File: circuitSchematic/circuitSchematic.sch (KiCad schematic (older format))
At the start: 7 parts, among them J1 MC912C128, U10 74LS138, U12 74HCT238, U14 OPT101, U15 KWM-30881AVB

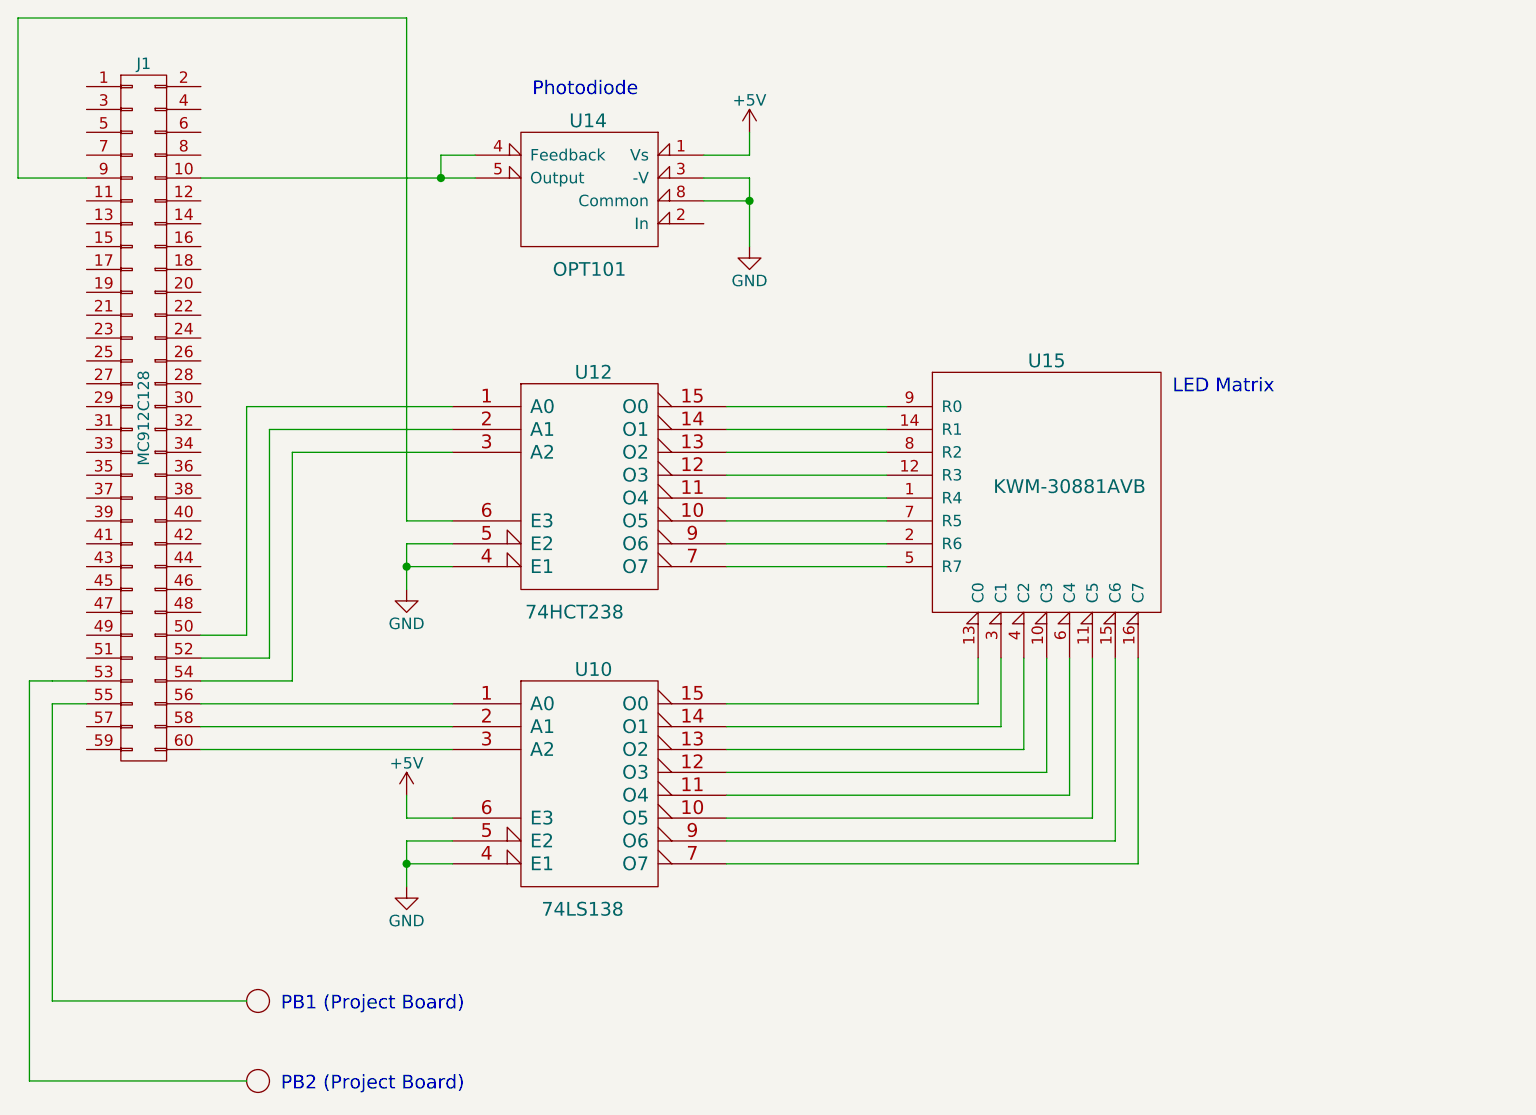
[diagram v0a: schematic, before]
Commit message: Added in the circuit schematic with resistors. Updated the kicad project appropiately.
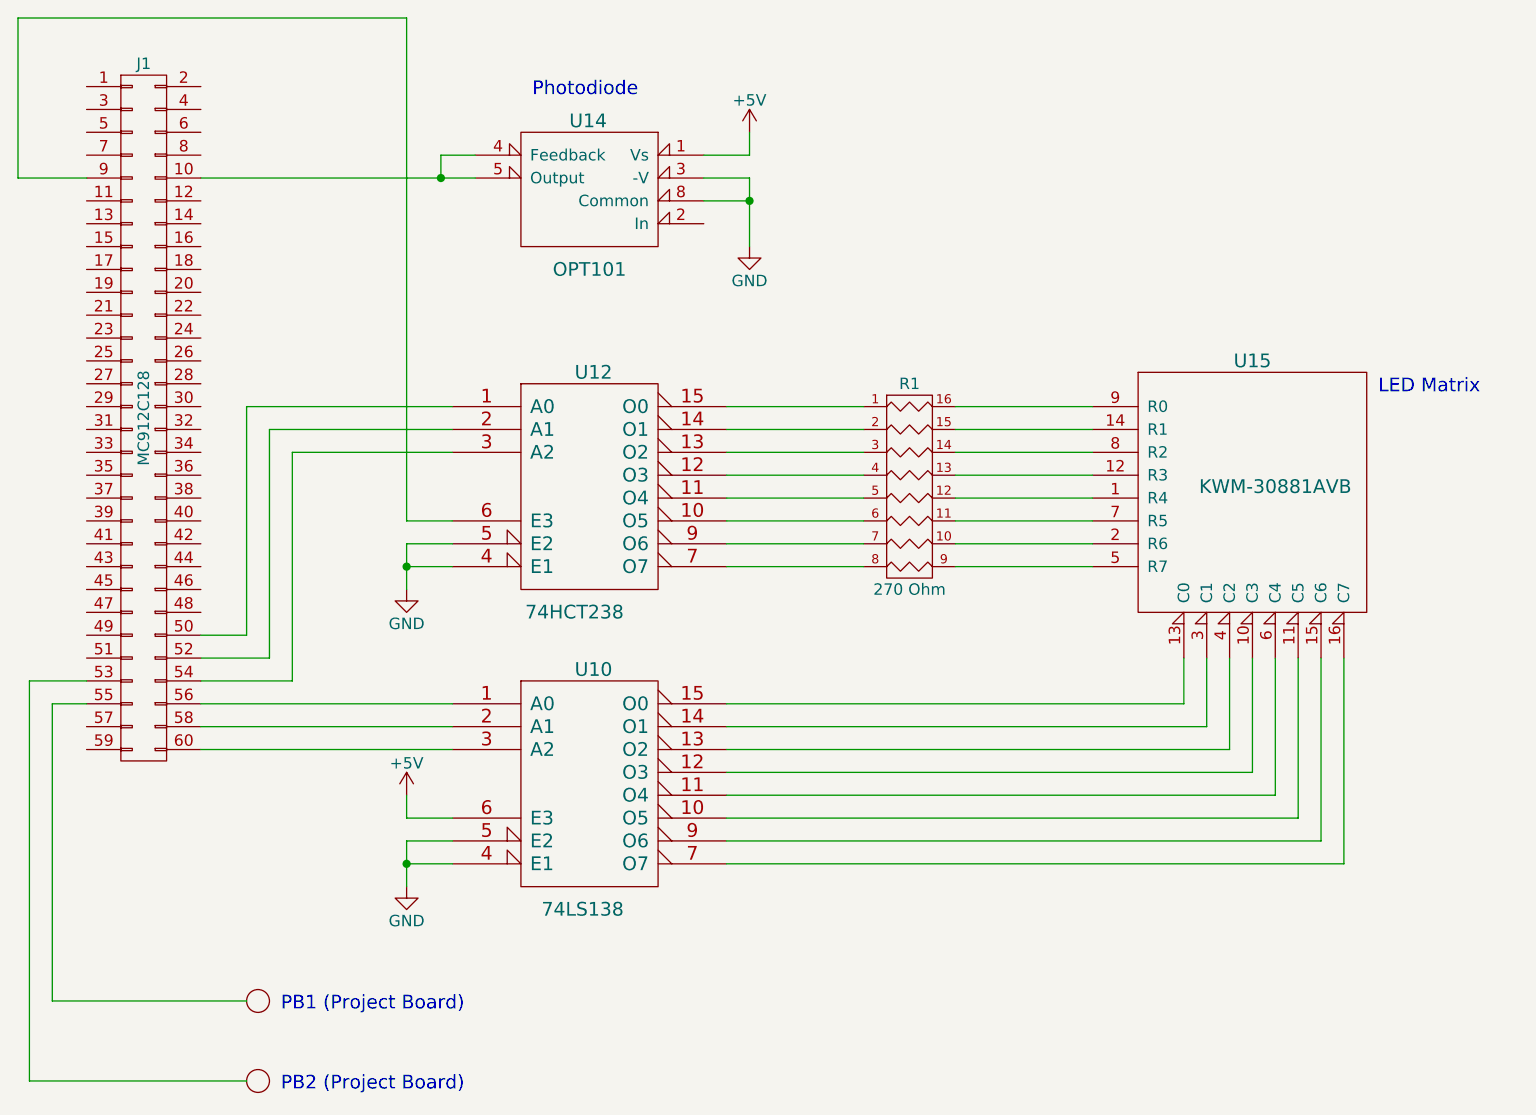
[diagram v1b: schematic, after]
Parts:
- added R1: 270 Ohm, symbol R_PACK8
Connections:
- wire segments 68 -> 71
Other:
- moved on the sheet: U15
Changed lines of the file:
@@
 L KWM-30881AVB U15
 U 1 1 554BE190
-P 5300 3650
-F 0 "U15" H 5300 4200 60  0000 C CNN
-F 1 "KWM-30881AVB" H 5400 3650 60  0000 C CNN
-F 2 "" H 5400 3650 60  0000 C CNN
-F 3 "" H 5400 3650 60  0000 C CNN
-	1    5300 3650
+P 6200 3650
+F 0 "U15" H 6200 4200 60  0000 C CNN
+F 1 "KWM-30881AVB" H 6300 3650 60  0000 C CNN
+F 2 "" H 6300 3650 60  0000 C CNN
+F 3 "" H 6300 3650 60  0000 C CNN
+	1    6200 3650
 	1    0    0    -1
 $EndComp
@@
 	1    0    0    -1
 $EndComp
-Text Notes 5850 3250 0    60   ~ 0
+Text Notes 6750 3250 0    60   ~ 0
 LED Matrix
 $Comp
@@
 	-1   0    0    -1
 $EndComp
-Wire Wire Line
-	1600 2300 2650 2300
-Wire Wire Line
-	2650 2300 2800 2300
-Wire Wire Line
-	850  6250 1800 6250
-Wire Wire Line
-	850  4500 850  6250
-Wire Wire Line
-	1100 4500 950  4500
-Wire Wire Line
-	950  4500 850  4500
-Wire Wire Line
-	950  5900 1800 5900
-Wire Wire Line
-	950  4600 950  5900
-Wire Wire Line
-	1100 4600 950  4600
-Wire Wire Line
-	2500 3800 2700 3800
-Wire Wire Line
-	2500 1600 2500 3800
-Wire Wire Line
-	800  1600 2500 1600
-Wire Wire Line
-	800  2300 800  1600
-Wire Wire Line
-	1100 2300 800  2300
-Connection ~ 2500 4000
-Wire Wire Line
-	2700 3900 2500 3900
-Wire Wire Line
-	2500 3900 2500 4000
-Wire Wire Line
-	2500 4000 2500 4100
-Wire Wire Line
-	2700 4000 2500 4000
-Wire Wire Line
-	2500 5100 2500 5000
-Wire Wire Line
-	2700 5100 2500 5100
-Connection ~ 2500 5300
-Wire Wire Line
-	2700 5200 2500 5200
-Wire Wire Line
-	2500 5200 2500 5300
-Wire Wire Line
-	2500 5300 2500 5400
-Wire Wire Line
-	2700 5300 2500 5300
-Wire Wire Line
-	1800 3300 2700 3300
-Wire Wire Line
-	1800 4300 1800 3300
-Wire Wire Line
-	1600 4300 1800 4300
-Wire Wire Line
-	1900 3400 2700 3400
-Wire Wire Line
-	1900 4400 1900 3400
-Wire Wire Line
-	1600 4400 1900 4400
-Wire Wire Line
-	2000 3500 2700 3500
-Wire Wire Line
-	2000 4500 2000 3500
-Wire Wire Line
-	1600 4500 2000 4500
-Wire Wire Line
-	1600 4600 2700 4600
-Wire Wire Line
-	1600 4700 2700 4700
-Wire Wire Line
-	1600 4800 2700 4800
-Wire Wire Line
-	5700 5300 5700 4400
-Wire Wire Line
-	3900 5300 5700 5300
-Wire Wire Line
-	5600 5200 5600 4400
-Wire Wire Line
-	3900 5200 5600 5200
-Wire Wire Line
-	5500 5100 5500 4400
-Wire Wire Line
-	3900 5100 5500 5100
-Wire Wire Line
-	5400 5000 5400 4400
-Wire Wire Line
-	3900 5000 5400 5000
-Wire Wire Line
-	5300 4900 5300 4400
-Wire Wire Line
-	3900 4900 5300 4900
-Wire Wire Line
-	5200 4800 5200 4400
-Wire Wire Line
-	3900 4800 5200 4800
-Wire Wire Line
-	5100 4700 5100 4400
-Wire Wire Line
-	3900 4700 5100 4700
-Wire Wire Line
-	5000 4600 5000 4400
-Wire Wire Line
-	3900 4600 5000 4600
-Wire Wire Line
-	3900 4000 4600 4000
-Wire Wire Line
-	3900 3900 4600 3900
-Wire Wire Line
-	3900 3800 4600 3800
-Wire Wire Line
-	3900 3700 4600 3700
-Wire Wire Line
-	3900 3600 4600 3600
-Wire Wire Line
-	3900 3500 4600 3500
-Wire Wire Line
-	3900 3400 4600 3400
-Wire Wire Line
-	3900 3300 4600 3300
-Wire Wire Line
-	2800 2200 2650 2200
-Wire Wire Line
-	2650 2200 2650 2300
-Connection ~ 2650 2300
 $Comp
 L GND #PWR?
@@
 	1    0    0    -1
 $EndComp
-Wire Wire Line
-	3800 2400 4000 2400
-Wire Wire Line
-	4000 2300 4000 2400
-Wire Wire Line
-	4000 2400 4000 2600
-Wire Wire Line
-	3800 2300 4000 2300
-Connection ~ 4000 2400
 $Comp
 L +5V #PWR?
@@
 	1    0    0    -1
 $EndComp
-Wire Wire Line
-	3800 2200 4000 2200
-Wire Wire Line
-	4000 2200 4000 2100
 Text Notes 3050 1950 0    60   ~ 0
 Photodiode
+Wire Wire Line
+	1600 2300 2800 2300
+Wire Wire Line
+	850  6250 1800 6250
+Wire Wire Line
+	850  4500 850  6250
+Wire Wire Line
+	850  4500 1100 4500
+Wire Wire Line
+	950  5900 1800 5900
+Wire Wire Line
+	950  4600 950  5900
+Wire Wire Line
+	1100 4600 950  4600
+Wire Wire Line
+	2500 3800 2700 3800
+Wire Wire Line
+	2500 1600 2500 3800
+Wire Wire Line
+	800  1600 2500 1600
+Wire Wire Line
+	800  2300 800  1600
+Wire Wire Line
+	1100 2300 800  2300
+Connection ~ 2500 4000
+Wire Wire Line
+	2700 3900 2500 3900
+Wire Wire Line
+	2500 3900 2500 4100
+Wire Wire Line
+	2700 4000 2500 4000
+Wire Wire Line
+	2500 5100 2500 5000
+Wire Wire Line
+	2700 5100 2500 5100
+Connection ~ 2500 5300
+Wire Wire Line
+	2700 5200 2500 5200
+Wire Wire Line
+	2500 5200 2500 5400
+Wire Wire Line
+	2700 5300 2500 5300
+Wire Wire Line
+	1800 3300 2700 3300
+Wire Wire Line
+	1800 4300 1800 3300
+Wire Wire Line
+	1600 4300 1800 4300
+Wire Wire Line
+	1900 3400 2700 3400
+Wire Wire Line
+	1900 4400 1900 3400
+Wire Wire Line
+	1600 4400 1900 4400
+Wire Wire Line
+	2000 3500 2700 3500
+Wire Wire Line
+	2000 4500 2000 3500
+Wire Wire Line
+	1600 4500 2000 4500
+Wire Wire Line
+	1600 4600 2700 4600
+Wire Wire Line
+	1600 4700 2700 4700
+Wire Wire Line
+	1600 4800 2700 4800
+Wire Wire Line
+	6600 5300 6600 4400
+Wire Wire Line
+	3900 5300 6600 5300
+Wire Wire Line
+	6500 5200 6500 4400
+Wire Wire Line
+	3900 5200 6500 5200
+Wire Wire Line
+	6400 5100 6400 4400
+Wire Wire Line
+	3900 5100 6400 5100
+Wire Wire Line
+	6300 5000 6300 4400
+Wire Wire Line
+	3900 5000 6300 5000
+Wire Wire Line
+	6200 4900 6200 4400
+Wire Wire Line
+	3900 4900 6200 4900
+Wire Wire Line
+	6100 4800 6100 4400
+Wire Wire Line
+	3900 4800 6100 4800
+Wire Wire Line
+	6000 4700 6000 4400
+Wire Wire Line
+	3900 4700 6000 4700
+Wire Wire Line
+	5900 4600 5900 4400
+Wire Wire Line
+	3900 4600 5900 4600
+Wire Wire Line
+	2800 2200 2650 2200
+Wire Wire Line
+	2650 2200 2650 2300
+Connection ~ 2650 2300
+Wire Wire Line
+	3800 2400 4000 2400
+Wire Wire Line
+	4000 2300 4000 2600
+Wire Wire Line
+	3800 2300 4000 2300
+Connection ~ 4000 2400
+Wire Wire Line
+	3800 2200 4000 2200
+Wire Wire Line
+	4000 2200 4000 2100
+$Comp
+L R_PACK8 R1
+U 1 1 555422F1
+P 4700 3650
+F 0 "R1" H 4700 4100 50  0000 C CNN
+F 1 "270 Ohm" H 4700 3200 50  0000 C CNN
+F 2 "" H 4700 3650 60  0000 C CNN
+F 3 "" H 4700 3650 60  0000 C CNN
+	1    4700 3650
+	1    0    0    -1
+$EndComp
+Wire Wire Line
+	3900 3300 4500 3300
+Wire Wire Line
+	4900 3300 5500 3300
+Wire Wire Line
+	3900 3400 4500 3400
+Wire Wire Line
+	4900 3400 5500 3400
+Wire Wire Line
+	3900 3500 4500 3500
+Wire Wire Line
+	4900 3500 5500 3500
+Wire Wire Line
+	3900 3600 4500 3600
+Wire Wire Line
+	4900 3600 5500 3600
+Wire Wire Line
+	4900 3700 5500 3700
+Wire Wire Line
+	3900 3700 4500 3700
+Wire Wire Line
+	3900 3800 4500 3800
+Wire Wire Line
+	4900 3800 5500 3800
+Wire Wire Line
+	3900 3900 4500 3900
+Wire Wire Line
+	4900 3900 5500 3900
+Wire Wire Line
+	3900 4000 4500 4000
+Wire Wire Line
+	4900 4000 5500 4000
 $EndSCHEMATC
